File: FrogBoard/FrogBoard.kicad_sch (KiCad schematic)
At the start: 61 parts, among them J1 Conn_01x10, J10 Conn_01x01, J11 Conn_01x01, J12 Conn_01x02, J13 Conn_01x01, J14 Conn_01x01, J15 Conn_01x01, J16 Conn_01x01, J17 Conn_01x01, J18 Conn_01x01, J19 Conn_01x01, J2 Conn_01x04, J20 Conn_01x01, J21 Conn_01x01, J22 Conn_01x01, J23 Conn_01x01, J24 Conn_01x01, J25 Conn_01x01, J27 Conn_01x01, J28 Conn_01x01, J3 USB_C_Receptacle_USB2.0_16P, J30 Conn_01x02, J4 Stickbox, J5 Conn_01x03_Socket, J6 Conn_01x02, J7 Conn_01x02, J8 Conn_01x01, J9 Conn_01x01, U1 STM32L432KBUx, U2 USBLC6-2P6, U3 MCP1700T-3302E, U4 BL1555

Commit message: Update footprint and put back micro USB
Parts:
- removed J3: USB_C_Receptacle_USB2.0_16P, FrogBoard_footprints:CONN16_C16PIN_SHN, symbol Connector:USB_C_Receptacle_USB2.0_16P
- removed R10, R8: 5.1k, Resistor_SMD:R_0603_1608Metric_Pad0.98x0.95mm_HandSolder, symbol Device:R
- added J26: USB_B_Micro, FrogBoard_footprints:AMPHENOL_10118194-0001LF, symbol Connector:USB_B_Micro
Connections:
- net GND: now also J26.5 (GND)
- net USB_RAW+: now also J26.3 (D+)
- net USB_RAW-: now also J26.2 (D-)
- net VBUS: now also J26.1 (VBUS)

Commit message: bulk rounting done
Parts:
- removed J12: Conn_01x02, FrogBoard_footprints:PinHeader_1x02_P1.00mm_Vertical_Neutral_No_Coutryard, symbol Connector_Generic:Conn_01x02
- added J12, J29, J3, J31, J32, J33: Conn_01x01, FrogBoard_footprints:FrogBoard_PinHeader_1x01_P1.00mm_Vertical, symbol Connector_Generic:Conn_01x01
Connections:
- net GND: now also J33.1 (Pin_1)
- net USB_RAW+: now also J31.1 (Pin_1)
- net USB_RAW-: now also J29.1 (Pin_1)
- net Unused_7: now also J3.1 (Pin_1)
- net Unused_8: now also J12.1 (Pin_1)
- net VBUS: now also J32.1 (Pin_1)
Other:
- moved on the sheet: J26

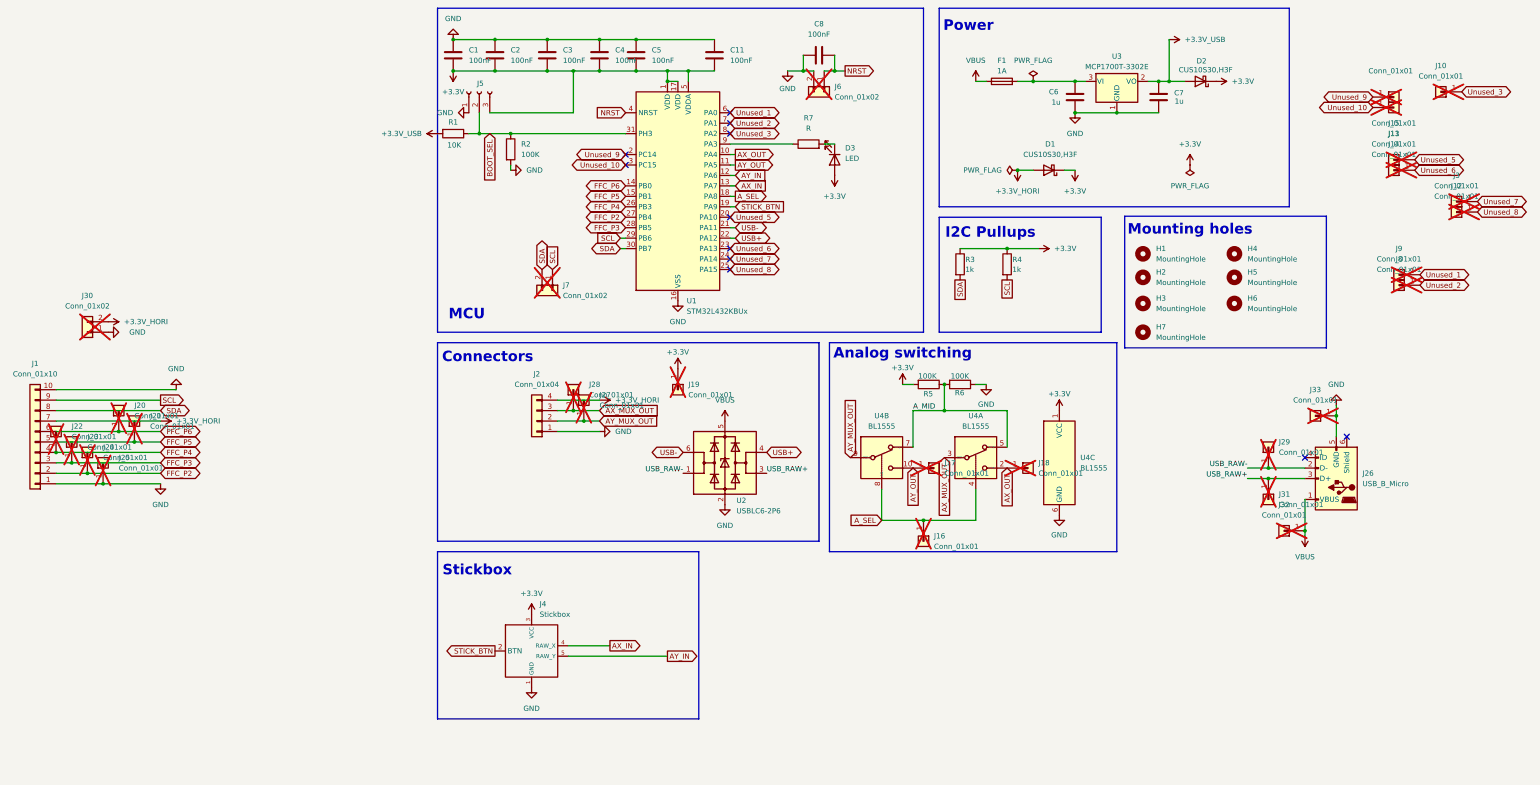
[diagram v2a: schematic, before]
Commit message: electrically correct
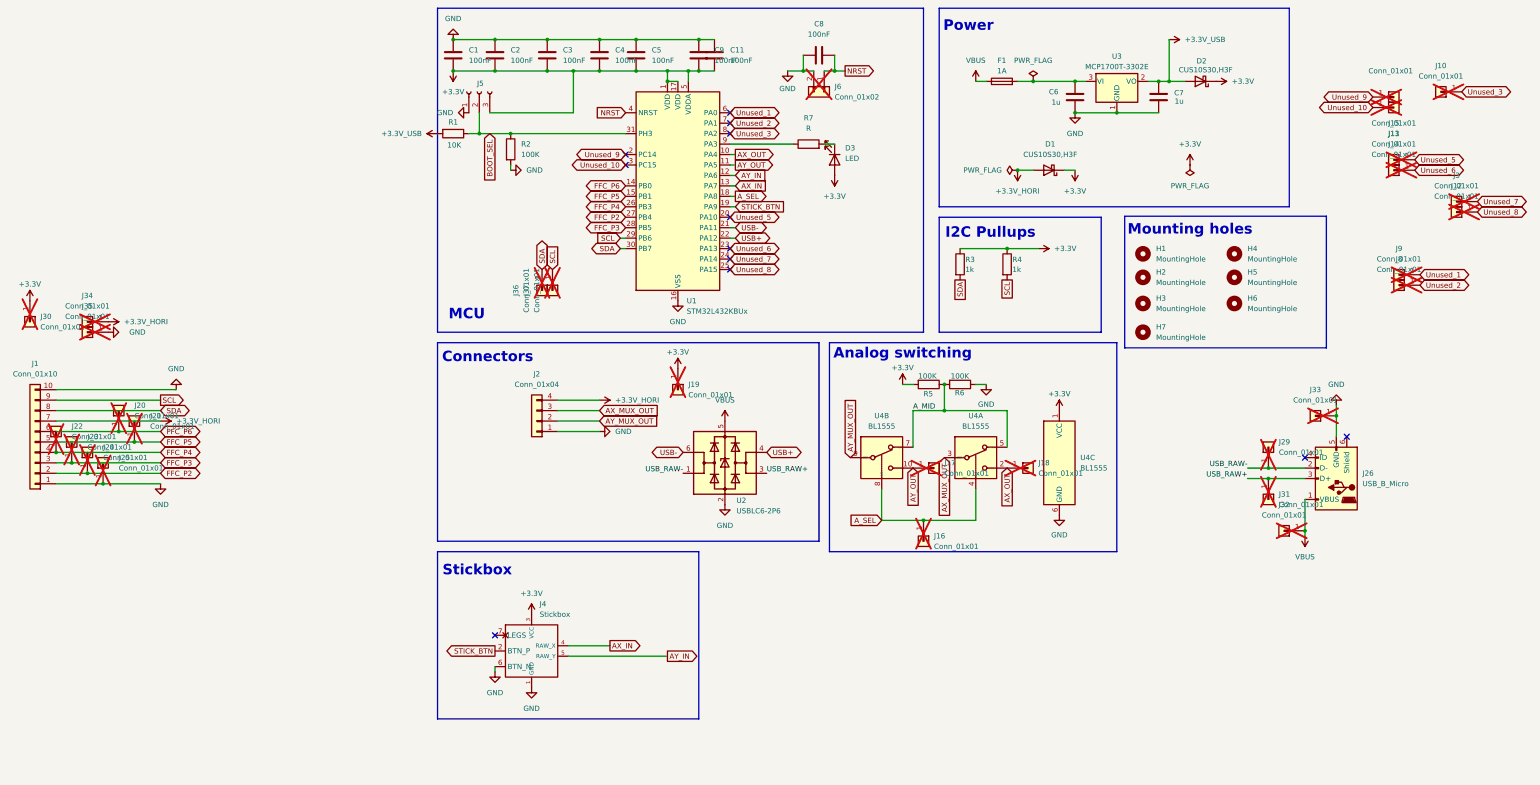
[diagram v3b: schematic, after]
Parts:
- removed J27, J28: Conn_01x01, FrogBoard_footprints:FrogBoard_PinHeader_1x01_P1.00mm_Vertical, symbol Connector_Generic:Conn_01x01
- removed J30, J7: Conn_01x02, FrogBoard_footprints:PinHeader_1x02_P1.00mm_Vertical_Neutral_No_Coutryard, symbol Connector_Generic:Conn_01x02
- added C9: 100nF, Capacitor_SMD:C_0603_1608Metric_Pad1.08x0.95mm_HandSolder, symbol Device:C
- added J30, J34, J35, J36, J37: Conn_01x01, FrogBoard_footprints:FrogBoard_PinHeader_1x01_P1.00mm_Vertical, symbol Connector_Generic:Conn_01x01
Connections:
- net +3.3V: now also C9.2, J30.1 (Pin_1)
- net +3.3V_HORI: now also J34.1 (Pin_1)
- net GND: now also J4.6 (BTN_N), C9.1, J35.1 (Pin_1)
- net SCL: now also J37.1 (Pin_1)
- net SDA: now also J36.1 (Pin_1)
- no-connect marks 11 -> 12

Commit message: Fix silkscreens
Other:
- moved on the sheet: J1, J20, J21, J22, J23, J24, J25, J30, J34, J35
